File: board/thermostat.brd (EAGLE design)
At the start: 39.4 x 50.8 mm, 14 parts, among them IC1 7805TV, Q1 PSMN4R3-30PL

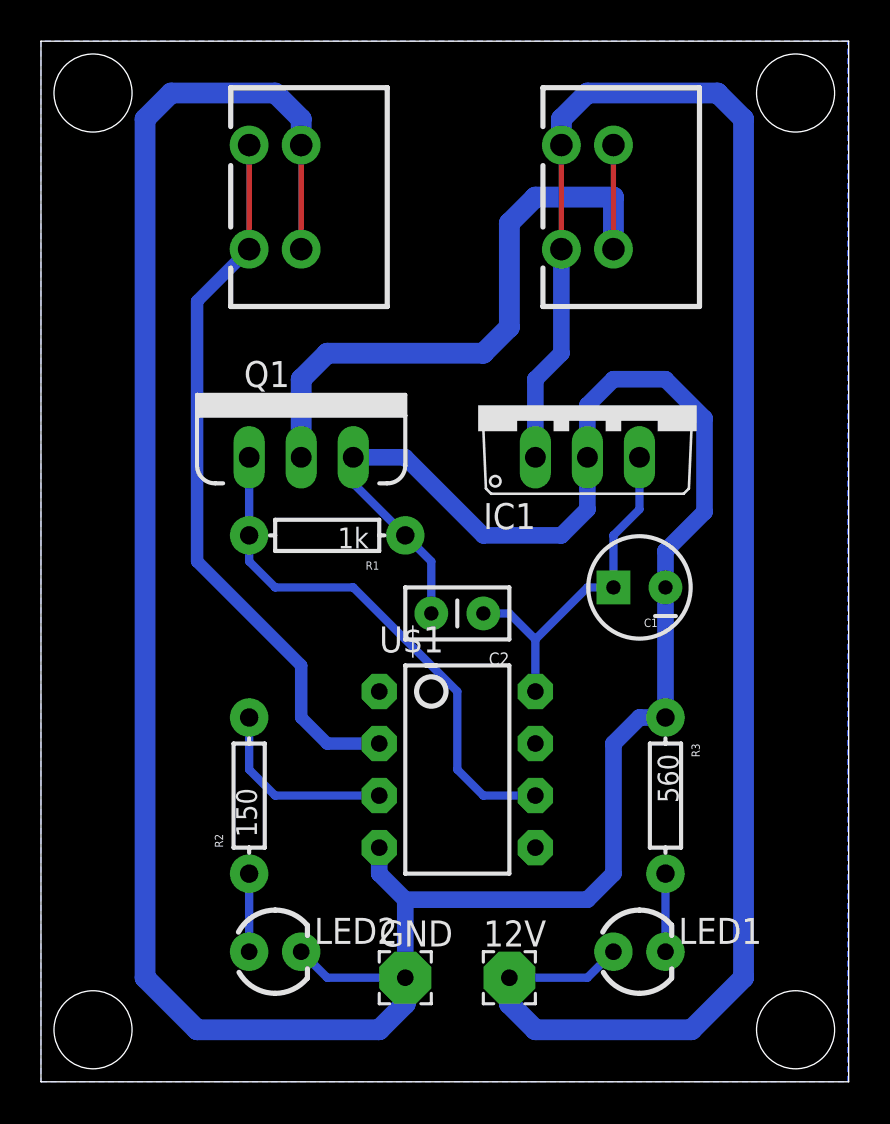
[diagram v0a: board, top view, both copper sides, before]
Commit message: WIP: Protecting input and creating schematic
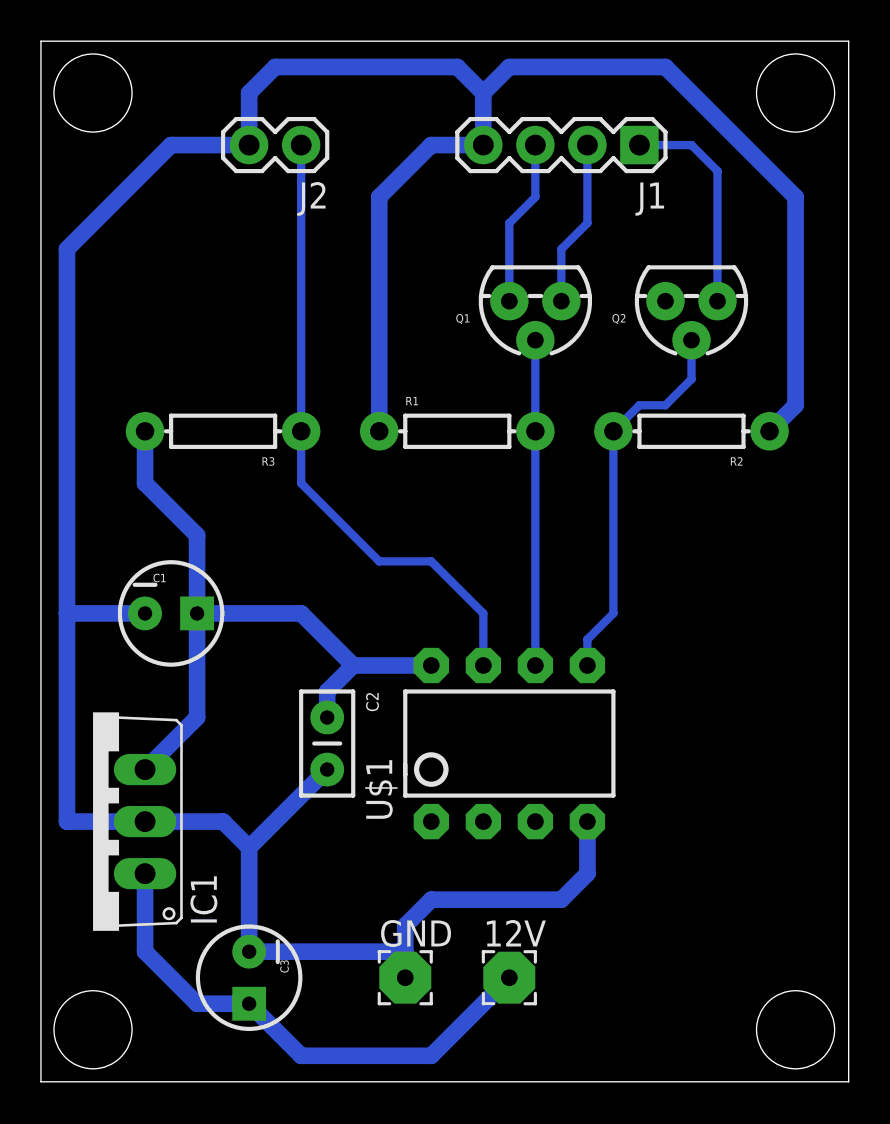
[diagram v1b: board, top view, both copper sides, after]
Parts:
- removed JP1, JP2: (no value), SparkFun-Connectors:SPRINGTERMINAL-2.54MM-2
- removed LED1, LED2: (no value), SparkFun-LED:LED3MM
- added C3: (no value), SparkFun-Capacitors:CPOL-RADIAL-10UF-25V
- added J1: (no value), SparkFun-Connectors:1X04
- added J2: (no value), SparkFun-Connectors:1X02
- added Q2: MOSFET-NCHANNEL2N7000, SparkFun-DiscreteSemi:TO-92
- Q1: value PSMN4R3-30PL -> MOSFET-NCHANNEL2N7000; device SparkFun-DiscreteSemi:TO220V -> SparkFun-DiscreteSemi:TO-92
- R1: value 1k -> (none)
- R2: value 150 -> (none)
- R3: value 560 -> (none)
- moved IC1 31.5 mm to (2.54, 12.7), turned to 90 degrees
- moved R2 28.0 mm to (31.8, 31.8), turned to 180 degrees
- moved R3 28.0 mm to (8.89, 31.8), turned to 180 degrees
- moved C1 22.9 mm to (6.35, 22.9), turned to 0 degrees
- moved Q1 13.7 mm to (24.1, 38.1), turned to 180 degrees
- moved C2 9.16 mm to (14.0, 17.8), turned to 270 degrees
- moved R1 8.13 mm to (20.3, 31.8), turned to 0 degrees
- moved U$1 2.84 mm to (22.9, 16.5), turned to 0 degrees
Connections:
- removed net DOOR_SW: JP2.2, U$1.2
- removed net LED_GND: JP1.1, Q1.2
- removed net N$1: LED1.K, R3.P$2
- removed net N$3: LED2.A, R2.P$1
- removed net PWM: Q1.1, R1.P$2, U$1.6
- removed net STATUS_LED: R2.P$2, U$1.3
- new net HEAT_OFF: Q2.2, R2.P$2, U$1.5
- new net HEAT_ON: Q1.2, R1.P$2, U$1.6
- new net SWITCH_OFF: J1.1, Q2.1
- new net SWITCH_ON: J1.2, Q1.1
- new net SW_COMMON: J1.3, Q1.3, Q2.3
- new net THERMOSTAT_IN: J2.1, R3.P$1, U$1.7
- net 12V: now also C3.1; no longer JP1.2, LED1.A
- net 5V: now also R3.P$2
- net GND: now also C3.2, J1.4, J2.2, R2.P$1; no longer JP2.1, LED2.K, Q1.3, R3.P$1
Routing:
- net 12V: track 83.7 -> 25.3 mm
- net THERMOSTAT_IN: track 0.00 -> 30.6 mm
- net DOOR_SW: track 30.4 -> 0.00 mm
- net LED_GND: track 28.2 -> 0.00 mm
- net PWM: track 26.0 -> 0.00 mm
- net HEAT_OFF: track 0.00 -> 18.7 mm
- net 5V: track 17.3 -> 34.2 mm
- net HEAT_ON: track 0.00 -> 15.9 mm
- net SWITCH_OFF: track 0.00 -> 10.7 mm
- net STATUS_LED: track 9.42 -> 0.00 mm
- net SWITCH_ON: track 0.00 -> 8.15 mm
- net SW_COMMON: track 0.00 -> 8.15 mm
- net N$3: track 3.81 -> 0.00 mm
- net N$1: track 3.81 -> 0.00 mm
- net GND: track 150.2 -> 150.7 mm
- removed copper zone on layer 16, net N$2

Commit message: Board layout updates
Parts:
- removed R3: (no value), SparkFun-Passives:AXIAL-0.3
- added Q3: MOSFET-NCHANNEL2N7000, SparkFun-DiscreteSemi:TO-92
- added R4: 100k, SparkFun-Passives:AXIAL-0.3
- added R5: 1k, SparkFun-Passives:AXIAL-0.3
- C1: value (none) -> 10uF
- C2, C3: value (none) -> 0.1uF
- R1, R2: value (none) -> 100k
- moved C2 1.27 mm to (15.2, 17.8)
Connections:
- new net N$1: Q3.2, R4.P$1, R5.P$1
- new net SENSOR_IN: Q3.3, U$1.7
- net 5V: now also R4.P$2; no longer R3.P$2
- net GND: now also Q3.1
- net THERMOSTAT_IN: now also R5.P$2; no longer R3.P$1, U$1.7
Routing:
- net SENSOR_IN: track 0.00 -> 48.4 mm
- net THERMOSTAT_IN: track 30.6 -> 5.61 mm
- net SW_COMMON: track 8.15 -> 25.0 mm
- net N$1: track 0.00 -> 12.4 mm
- net 5V: track 34.2 -> 29.8 mm
- net GND: track 150.7 -> 154.6 mm
- net SWITCH_OFF: track 10.7 -> 9.20 mm
- net HEAT_OFF: track 18.7 -> 18.0 mm
- net 12V: track 25.3 -> 25.9 mm
- added copper zone on layer 16, net N$2
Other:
- board size 39.4 x 50.8 mm -> 38.2 x 50.8 mm

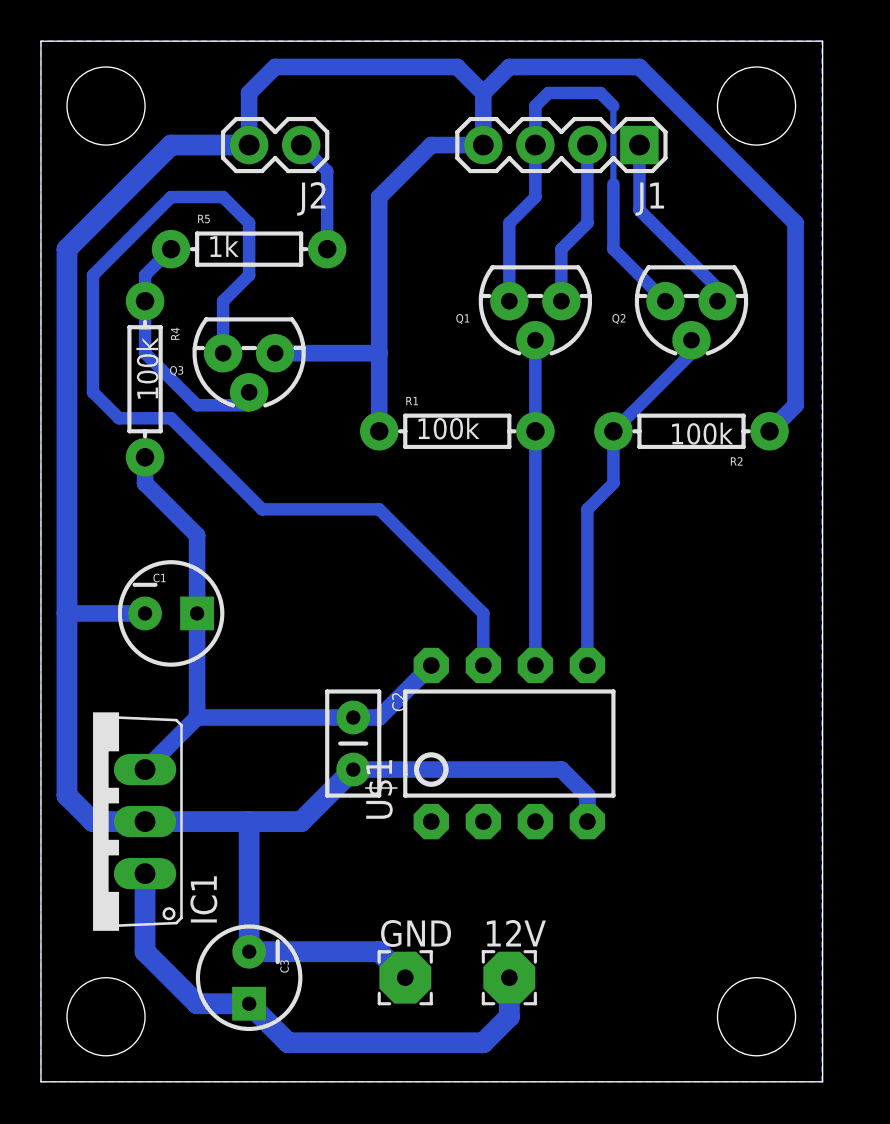
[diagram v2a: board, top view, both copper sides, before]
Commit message: Production build & source
The Thermostat relay board is successfully working in the spare bedroom.
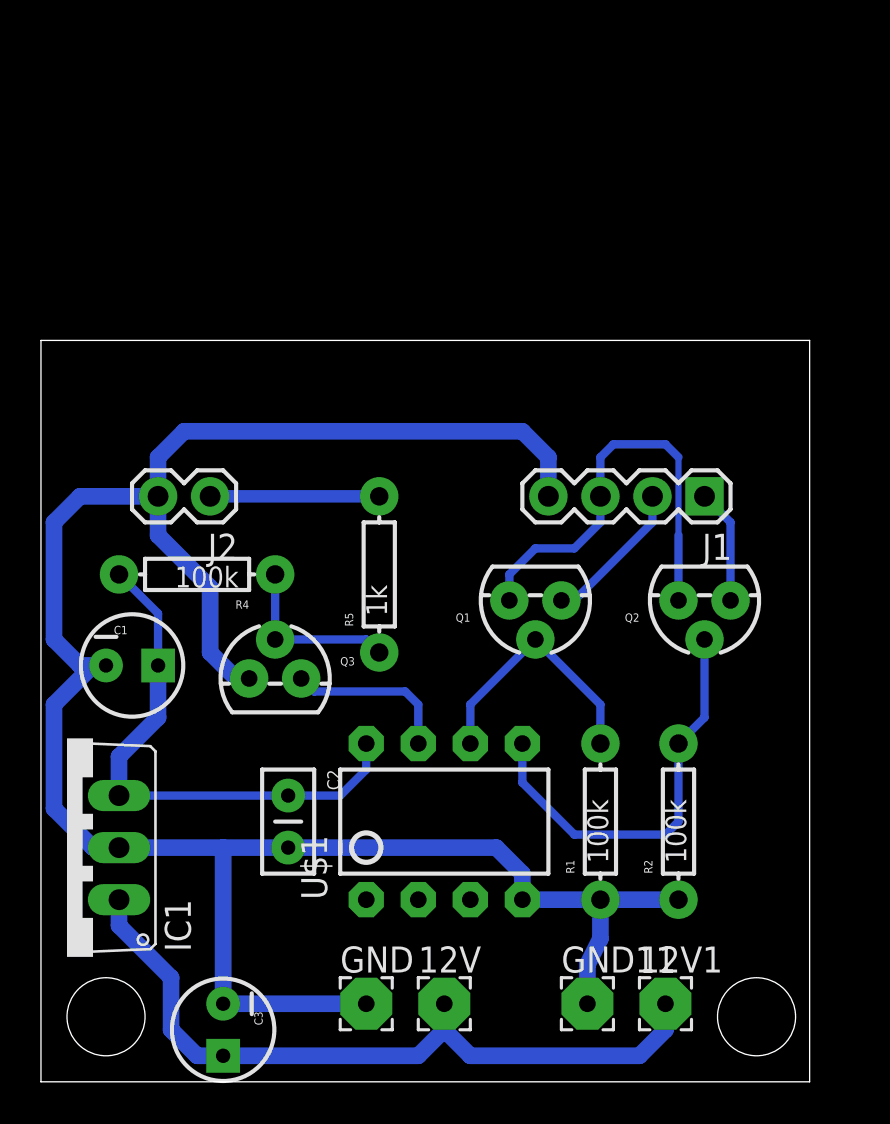
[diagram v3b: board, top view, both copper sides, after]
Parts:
- added 12V1, GND11: (no value), wirepad:2,54/0,8
- moved R1 20.3 mm to (27.3, 12.7), turned to 90 degrees
- moved R2 19.1 mm to (31.1, 12.7), turned to 90 degrees
- moved J2 17.7 mm to (8.26, 28.6)
- moved J1 17.4 mm to (32.4, 28.6)
- moved R5 17.1 mm to (16.5, 24.8), turned to 90 degrees
- moved Q3 15.9 mm to (11.4, 19.7), turned to 0 degrees
- moved Q2 14.6 mm to (32.4, 23.5)
- moved Q1 14.6 mm to (24.1, 23.5)
- moved R4 9.86 mm to (7.62, 24.8), turned to 180 degrees
- moved U$1 4.96 mm to (19.7, 12.7)
- moved C2 4.96 mm to (12.1, 14.0)
- moved 12V 3.42 mm to (19.7, 3.81)
- moved C1 3.17 mm to (4.45, 20.3)
- moved C3 2.84 mm to (8.89, 2.54)
- moved GND 2.29 mm to (15.9, 3.81)
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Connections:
- net 12V: now also 12V1.1
- net GND: now also GND11.1
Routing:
- net GND: track 154.6 -> 110.7 mm
- net SENSOR_IN: track 48.4 -> 8.15 mm
- net 12V: track 25.9 -> 36.2 mm
- net N$1: track 12.4 -> 8.52 mm
- net SW_COMMON: track 25.0 -> 21.3 mm
- net 5V: track 29.8 -> 26.2 mm
- net SWITCH_OFF: track 9.20 -> 5.61 mm
- net HEAT_ON: track 15.9 -> 12.8 mm
- net THERMOSTAT_IN: track 5.61 -> 8.26 mm
- net HEAT_OFF: track 18.0 -> 20.3 mm
- net SWITCH_ON: track 8.15 -> 7.29 mm
- removed copper zone on layer 16, net N$2
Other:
- board size 38.2 x 50.8 mm -> 37.5 x 36.2 mm
